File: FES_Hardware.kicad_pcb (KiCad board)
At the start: 4 copper layers, 55 parts, among them J1 Screw_Terminal_01x02, Q1 STD5N20L, Q2 STD5N20L, Q3 STD5N20L, Q4 STD5N20L, SW1 SW_Rotary_1x8_MP, U1 LM2586S, U2 TPS63802DLAR, U3 ESP32-DEVKITC-32UE, U4 IRS2005M, U5 IRS2005M

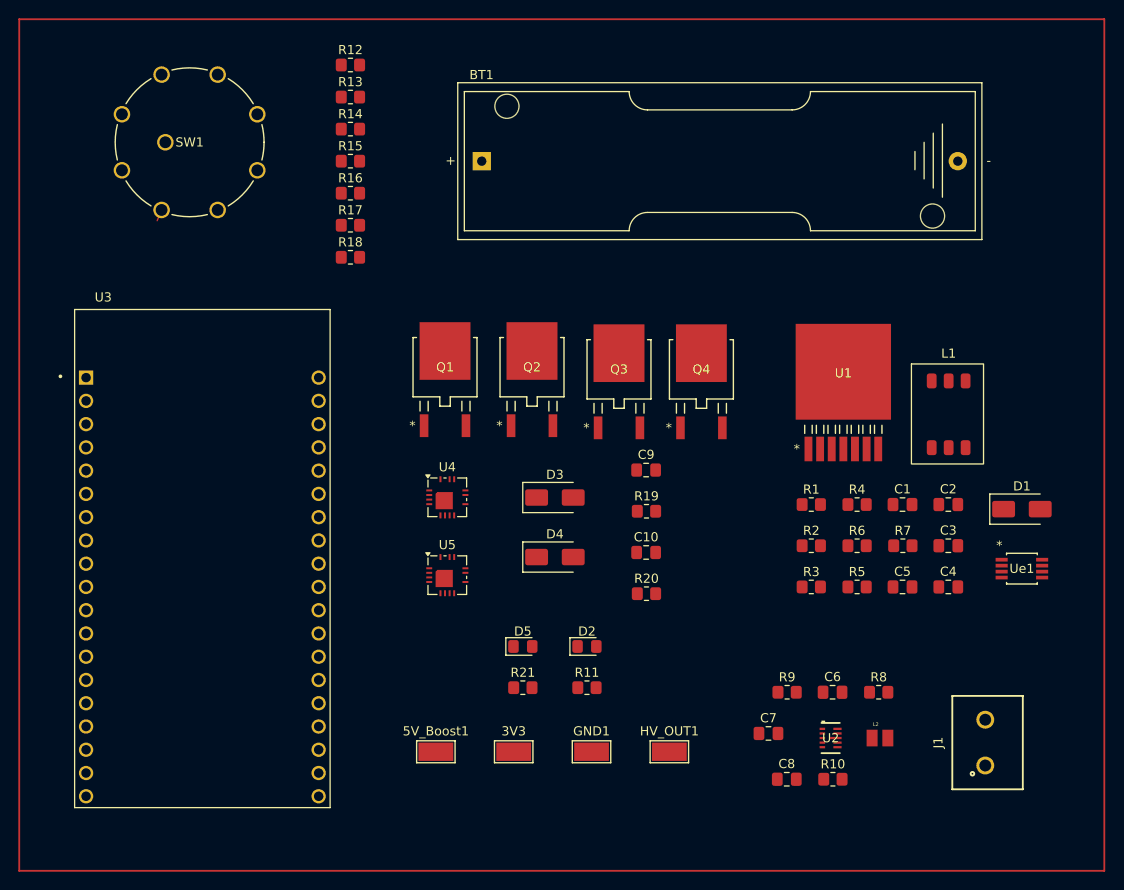
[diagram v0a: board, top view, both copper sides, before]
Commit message: routed PCB and added status LED for 5V
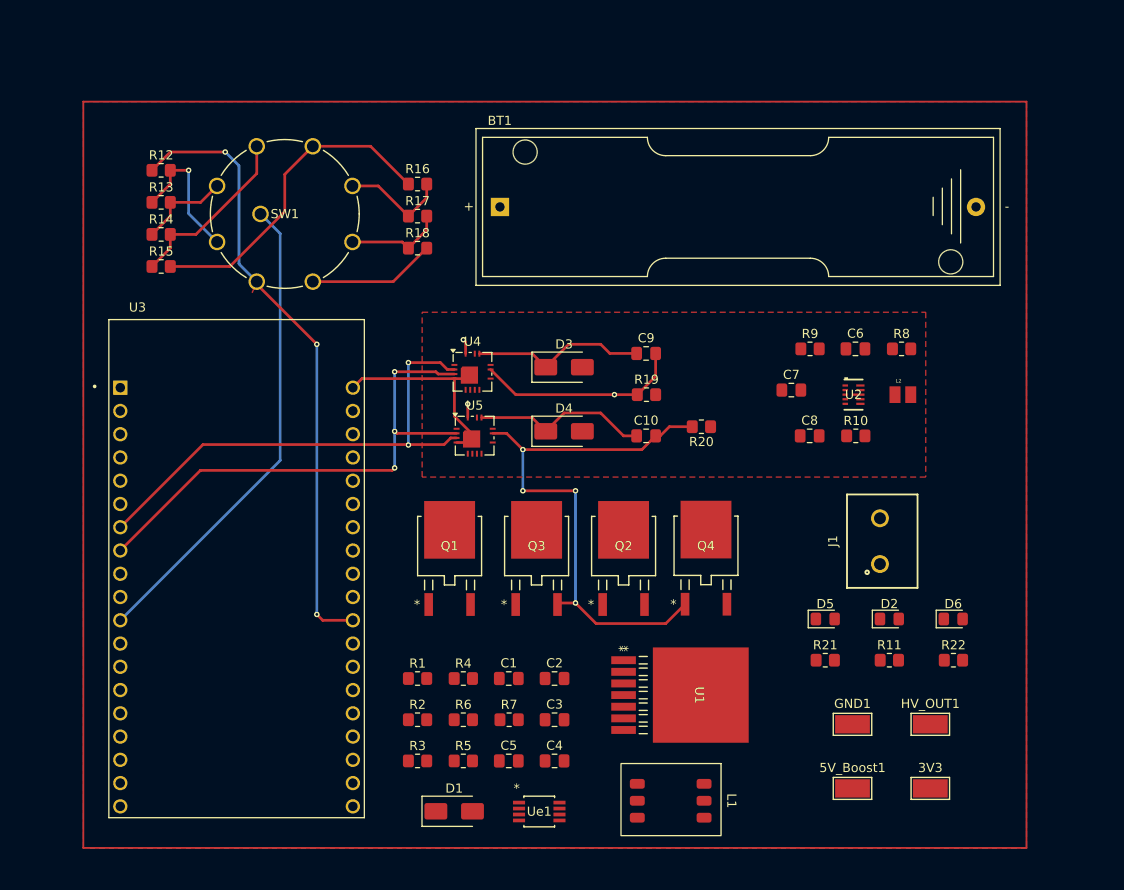
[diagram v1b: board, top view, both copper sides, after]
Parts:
- added D6: LED, LED_SMD:LED_0805_2012Metric_Pad1.15x1.40mm_HandSolder, F.Cu at (180.5, 130.5)
- added R22: 150, Resistor_SMD:R_0805_2012Metric_Pad1.20x1.40mm_HandSolder, F.Cu at (180.5, 135.0)
- moved D1 70.2 mm to (126.0, 151.5)
- moved Ue1 59.0 mm to (135.3, 151.5)
- moved L1 52.1 mm to (150.1, 150.3), turned to -90 degrees
- moved C1 47.0 mm to (132.0, 137.0)
- moved C2 47.0 mm to (137.0, 137.0)
- moved C3 47.0 mm to (137.0, 141.5)
- moved C4 47.0 mm to (137.0, 146.0)
- moved C5 47.0 mm to (132.0, 146.0)
- moved R1 47.0 mm to (122.0, 137.0)
- moved R2 47.0 mm to (122.0, 141.5)
- moved R3 47.0 mm to (122.0, 146.0)
- moved R4 47.0 mm to (127.0, 137.0)
- moved R5 47.0 mm to (127.0, 146.0)
- moved R6 47.0 mm to (127.0, 141.5)
- moved R7 47.0 mm to (132.0, 141.5)
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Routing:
- net ROT_3V3: track 0.00 -> 67.4 mm, vias 0 -> 3
- net Net-(Q3-S): track 0.00 -> 61.9 mm, vias 0 -> 4
- net DRV_B: track 0.00 -> 57.7 mm, vias 0 -> 3
- net DRV_A: track 0.00 -> 55.1 mm, vias 0 -> 2
- net ROT_SW: track 0.00 -> 52.5 mm
- net GND: track 0.00 -> 36.4 mm
- net Net-(R15-Pad2): track 0.00 -> 35.5 mm
- net Net-(Q1-S): track 0.00 -> 22.5 mm, vias 0 -> 1
- net Net-(R14-Pad2): track 0.00 -> 19.5 mm
- net Net-(D4-K): track 0.00 -> 19.4 mm
- net Net-(D3-K): track 0.00 -> 19.2 mm
- net Net-(R12-Pad2): track 0.00 -> 15.4 mm, vias 0 -> 1
- net Net-(R16-Pad2): track 0.00 -> 11.8 mm
- net Net-(R17-Pad2): track 0.00 -> 10.7 mm
- net Net-(R13-Pad2): track 0.00 -> 10.2 mm
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- added copper zone on F.Cu, net +5V
- added copper zone on B.Cu, net GND
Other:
- copper layers 4 -> 2

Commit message: ryanPCB branch commit for pcb layout
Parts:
- moved HV_OUT1 11.2 mm to (166.8, 142.0)
- moved GND1 8.50 mm to (178.0, 142.0)
- moved 5V_Boost1 2.75 mm to (166.8, 149.0)
- moved U1 1.84 mm to (154.6, 138.8)
- moved BT1 1.76 mm to (129.3, 85.2)
- moved J1 1.25 mm to (172.5, 120.8)
- moved C5 0.07 mm to (132.0, 146.0)
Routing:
- net +5V: track 3.13 -> 239.7 mm, vias 2 -> 12
- net GND: track 36.4 -> 197.8 mm, vias 0 -> 12
- net ROT_3V3: track 67.4 -> 146.9 mm, vias 3 -> 4
- net DRV_A: track 55.1 -> 129.6 mm, vias 2 -> 5
- net DRV_B: track 57.7 -> 119.3 mm, vias 3 -> 5
- net ESP32_SCL: track 0.00 -> 57.5 mm, vias 0 -> 5
- net Net-(BT1-+): track 0.00 -> 54.4 mm, vias 0 -> 2
- net ESP32_SDA: track 0.00 -> 53.8 mm, vias 0 -> 5
- net Net-(U1-FB): track 0.00 -> 52.1 mm, vias 0 -> 5
- net HV_OUT: track 0.00 -> 47.8 mm, vias 0 -> 3
- net Net-(Q2-G): track 0.00 -> 43.6 mm, vias 0 -> 2
- net Net-(Q1-S): track 22.5 -> 63.6 mm, vias 1 -> 4
- net Net-(U1-COMP): track 0.00 -> 33.6 mm, vias 0 -> 2
- net Net-(U1-~ON/OFF): track 0.00 -> 33.3 mm, vias 0 -> 2
- net Net-(Q4-G): track 0.00 -> 33.1 mm, vias 0 -> 2
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- added copper zone on In2.Cu, net +5V
- added copper zone on In1.Cu, net GND
- added copper zone on In2.Cu, net HV_OUT
- removed copper zone on F.Cu, net +5V
- removed copper zone on B.Cu, net GND
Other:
- board outline added: 100 x 80 mm
- copper layers 2 -> 4

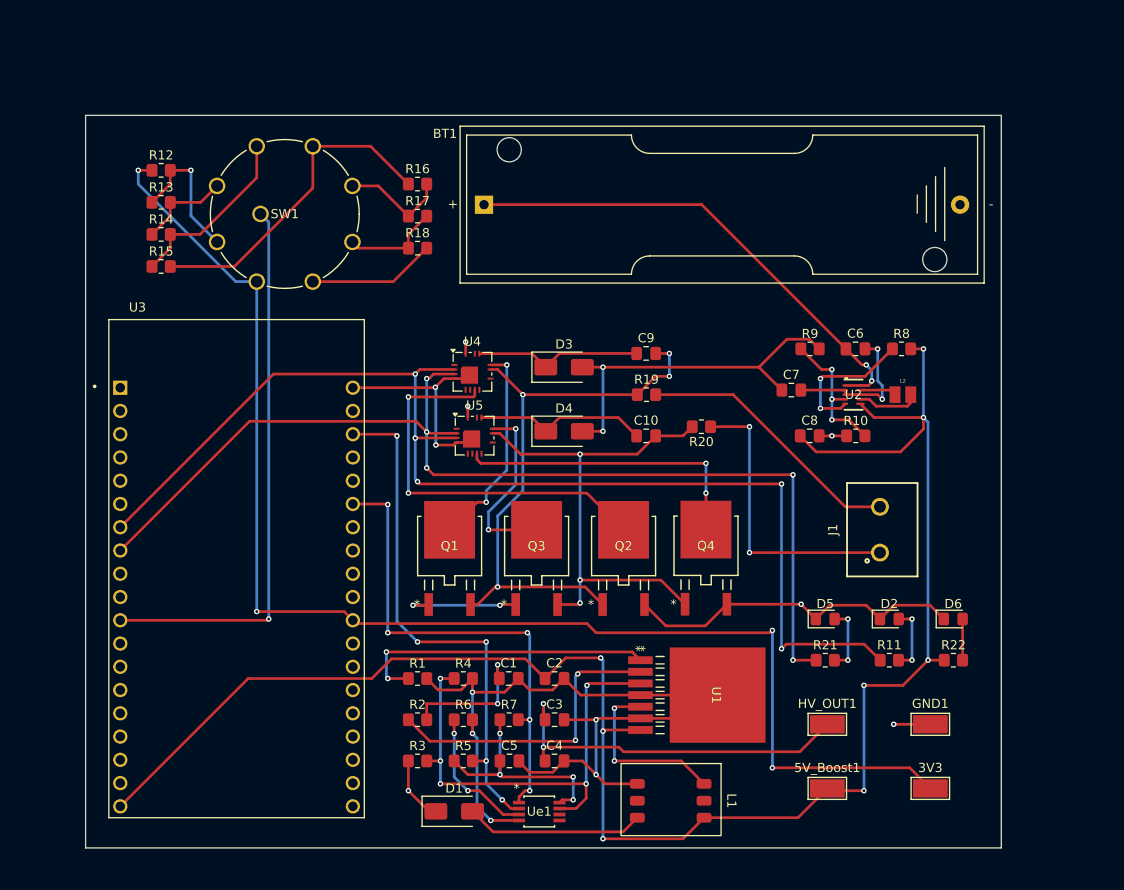
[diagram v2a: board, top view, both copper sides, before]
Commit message: tidied up PCB routing, renamed HV_OUT, changed MCU footprint/schematic
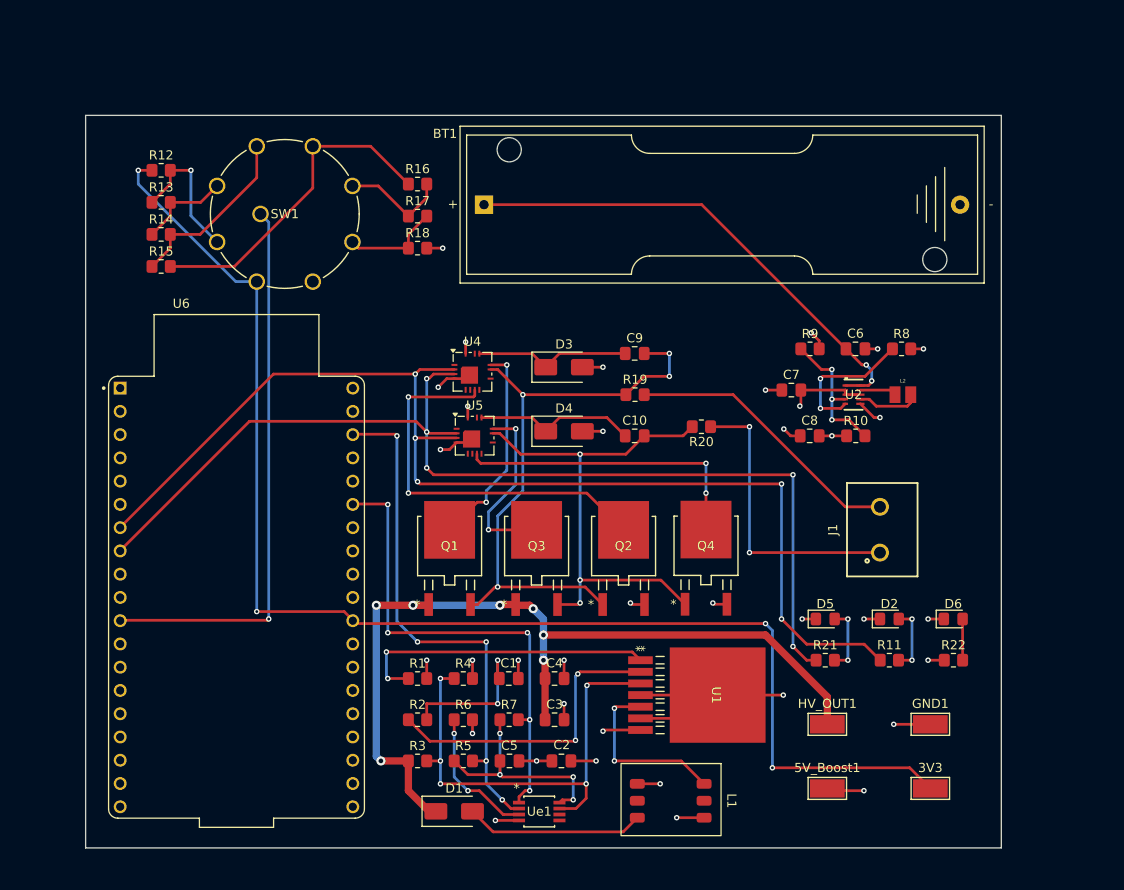
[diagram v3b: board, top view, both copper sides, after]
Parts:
- removed U3: ESP32-DEVKITC-32UE, ESP32-DEVKITC_32UE:ESPRESSIF_ESP32-DEVKITC-32UE
- added U6: ESP32-DEVKITC-32E, ESP32-DEVKITC-32E:MODULE_ESP32-DEVKITC-32E, F.Cu at (102.2, 128.1)
- moved C2 9.03 mm to (137.7, 146.0), turned to 180 degrees
- moved C4 9.00 mm to (137.0, 137.0)
- moved C10 1.25 mm to (145.7, 110.5)
- moved C9 1.25 mm to (145.7, 101.5)
- moved R19 1.25 mm to (145.8, 106.0)
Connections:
- Q1 pad 1: HV_Out -> HV_OUT
- Q3 pad 1: HV_Out -> HV_OUT
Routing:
- net +5V: track 239.7 -> 32.9 mm, vias 12 -> 14
- net GND: track 197.8 -> 83.3 mm, vias 12 -> 22
- net HV_OUT: track 47.8 -> 95.9 mm, vias 3 -> 7
- net HV_Out: track 13.0 -> 0.00 mm, vias 2 -> 0
- net DRV_A: track 129.6 -> 127.2 mm
- net P_Elec: track 29.6 -> 30.8 mm
- net Net-(Q1-S): track 63.6 -> 64.9 mm
- net Net-(D4-K): track 19.0 -> 17.8 mm
- net Net-(D3-K): track 18.4 -> 17.2 mm
- net Net-(C1-Pad1): track 15.3 -> 16.3 mm
- net DRV_B: track 119.3 -> 118.4 mm
- removed copper zone on In2.Cu, net HV_OUT

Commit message: added decoupling caps to MCU 5V input
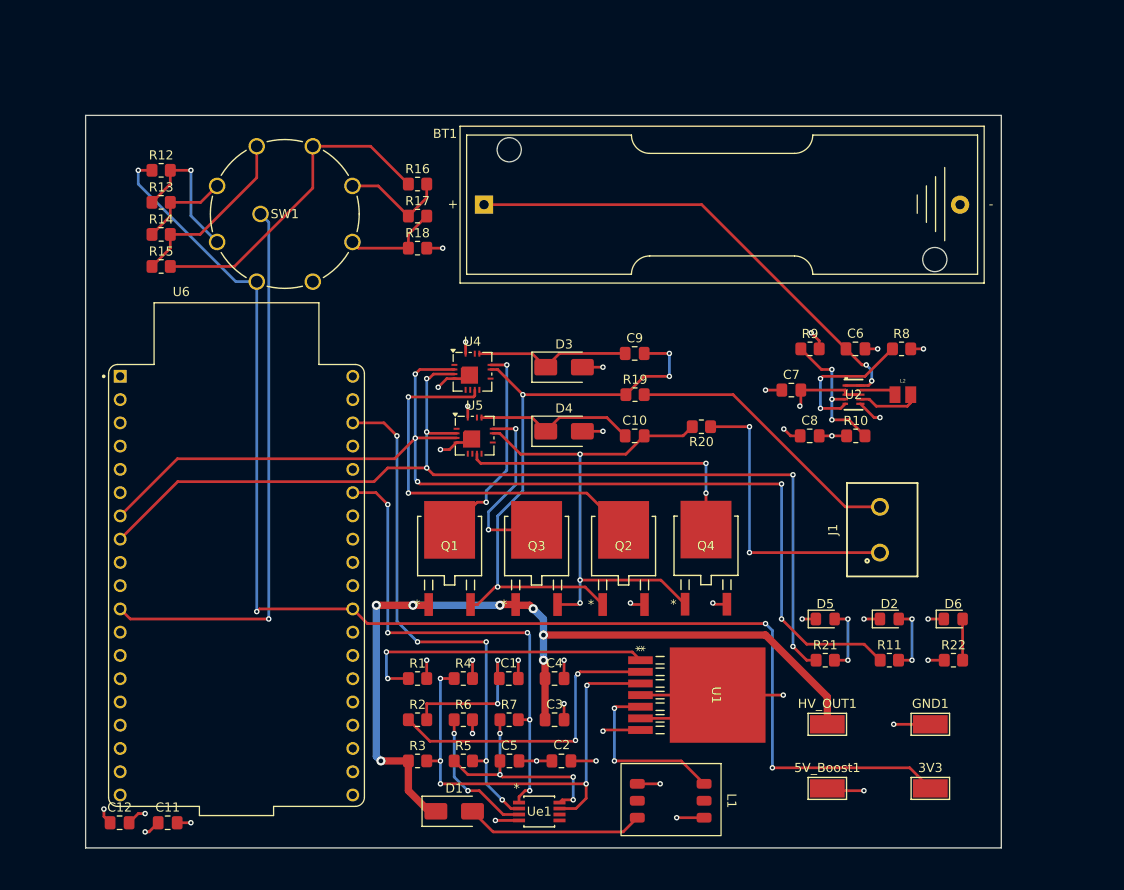
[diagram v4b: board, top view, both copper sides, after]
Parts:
- added C11: 10uF, Capacitor_SMD:C_0805_2012Metric_Pad1.18x1.45mm_HandSolder, F.Cu at (94.7, 152.8)
- added C12: .1uF, Capacitor_SMD:C_0805_2012Metric_Pad1.18x1.45mm_HandSolder, F.Cu at (89.5, 152.8)
- moved U6 1.29 mm to (102.2, 126.8)
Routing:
- net GND: track 83.3 -> 86.9 mm, vias 22 -> 24
- net +5V: track 32.9 -> 36.5 mm, vias 14 -> 16
- net DRV_A: track 127.2 -> 123.8 mm
- net DRV_B: track 118.4 -> 115.3 mm
- net ESP32_SDA: track 53.8 -> 54.3 mm
- net ESP32_SCL: track 57.5 -> 58.0 mm
